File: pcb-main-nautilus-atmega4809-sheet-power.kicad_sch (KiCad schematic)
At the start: 14 parts, among them U1 NCP1117-5.0_TO252, U2 AP2112K-3.3

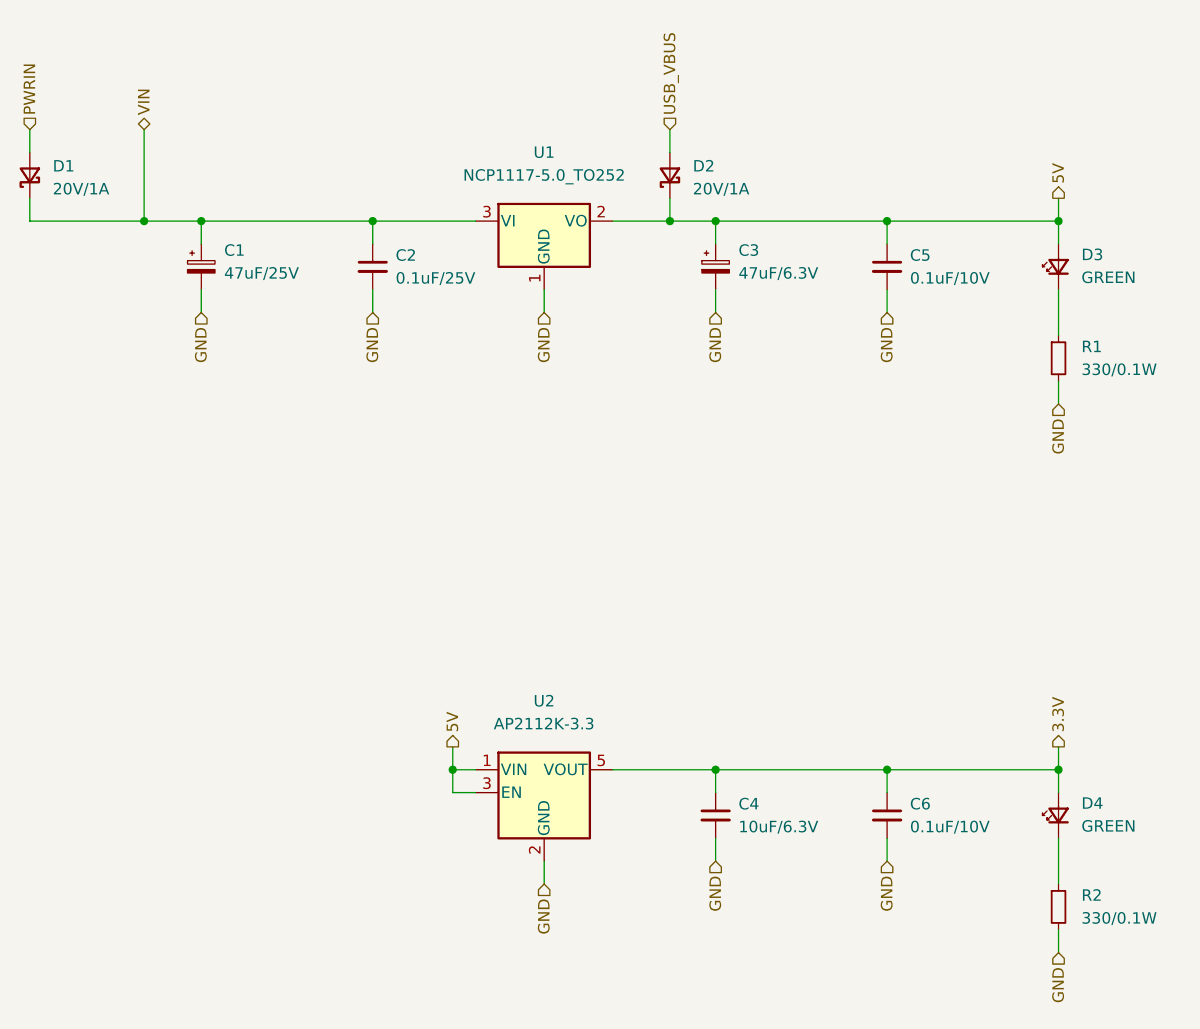
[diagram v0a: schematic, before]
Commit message: Add UPDI programmer and USB-serial bridge sheet
Supports #2.
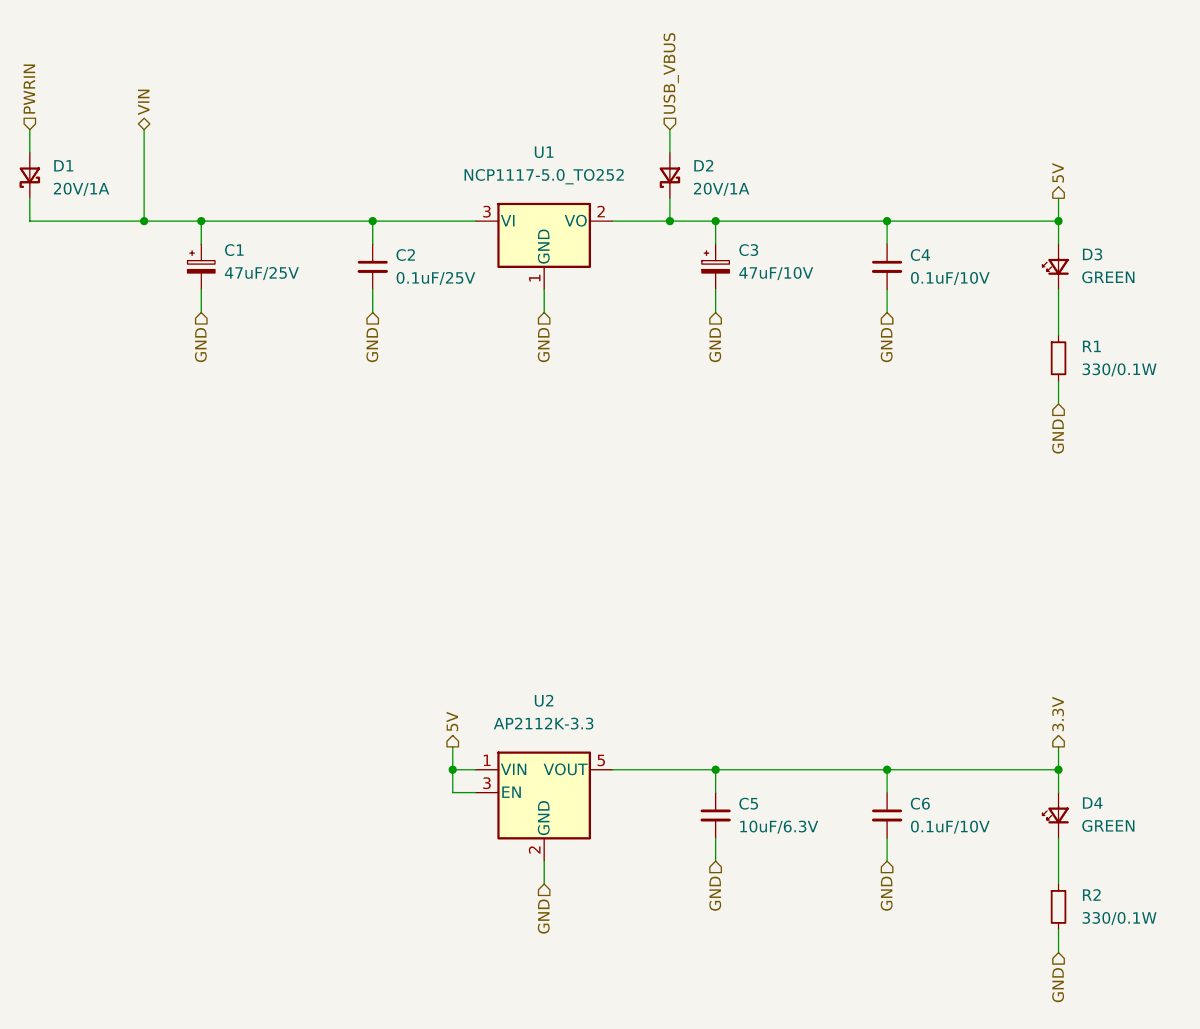
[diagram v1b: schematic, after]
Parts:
- C3: value 47uF/6.3V -> 47uF/10V; Digi-Key Part Number PCE3769CT-ND -> 10-EEE-FN1A470URCT-ND; Manufacturer Part Number EEE-FK0J470R -> EEE-FN1A470UR; Mouser Part Number 667-EEE-FK0J470R -> 667-EEE-FN1A470UR
- renumbered C5 to C4, C4 to C5
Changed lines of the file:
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@@
       (effects (font (size 1.27 1.27)) (justify left))
     )
-    (property "Value" "47uF/6.3V" (id 1) (at 161.29 75.6538 0)
+    (property "Value" "47uF/10V" (id 1) (at 161.29 75.6538 0)
       (effects (font (size 1.27 1.27)) (justify left))
     )
@@
       (effects (font (size 1.27 1.27)) hide)
     )
-    (property "Manufacturer Part Number" "EEE-FK0J470R" (id 5) (at 158.75 74.93 0)
+    (property "Manufacturer Part Number" "EEE-FN1A470UR" (id 5) (at 158.75 74.93 0)
       (effects (font (size 1.27 1.27)) hide)
     )
-    (property "Digi-Key Part Number" "PCE3769CT-ND" (id 6) (at 158.75 74.93 0)
+    (property "Digi-Key Part Number" "10-EEE-FN1A470URCT-ND" (id 6) (at 158.75 74.93 0)
       (effects (font (size 1.27 1.27)) hide)
     )
-    (property "Mouser Part Number" "667-EEE-FK0J470R" (id 7) (at 158.75 74.93 0)
+    (property "Mouser Part Number" "667-EEE-FN1A470UR" (id 7) (at 158.75 74.93 0)
       (effects (font (size 1.27 1.27)) hide)
     )
@@
   (symbol (lib_id "Device:C_Small") (at 177.8 74.93 0) (unit 1)
     (in_bom yes) (on_board yes) (fields_autoplaced)
-    (property "Reference" "C5" (id 0) (at 180.34 73.6662 0)
+    (property "Reference" "C4" (id 0) (at 180.34 73.6662 0)
       (effects (font (size 1.27 1.27)) (justify left))
     )
@@
   (symbol (lib_id "Device:C_Small") (at 158.75 135.89 0) (unit 1)
     (in_bom yes) (on_board yes) (fields_autoplaced)
-    (property "Reference" "C4" (id 0) (at 161.29 134.6262 0)
+    (property "Reference" "C5" (id 0) (at 161.29 134.6262 0)
       (effects (font (size 1.27 1.27)) (justify left))
     )
